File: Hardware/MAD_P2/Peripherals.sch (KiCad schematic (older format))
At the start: 24 parts

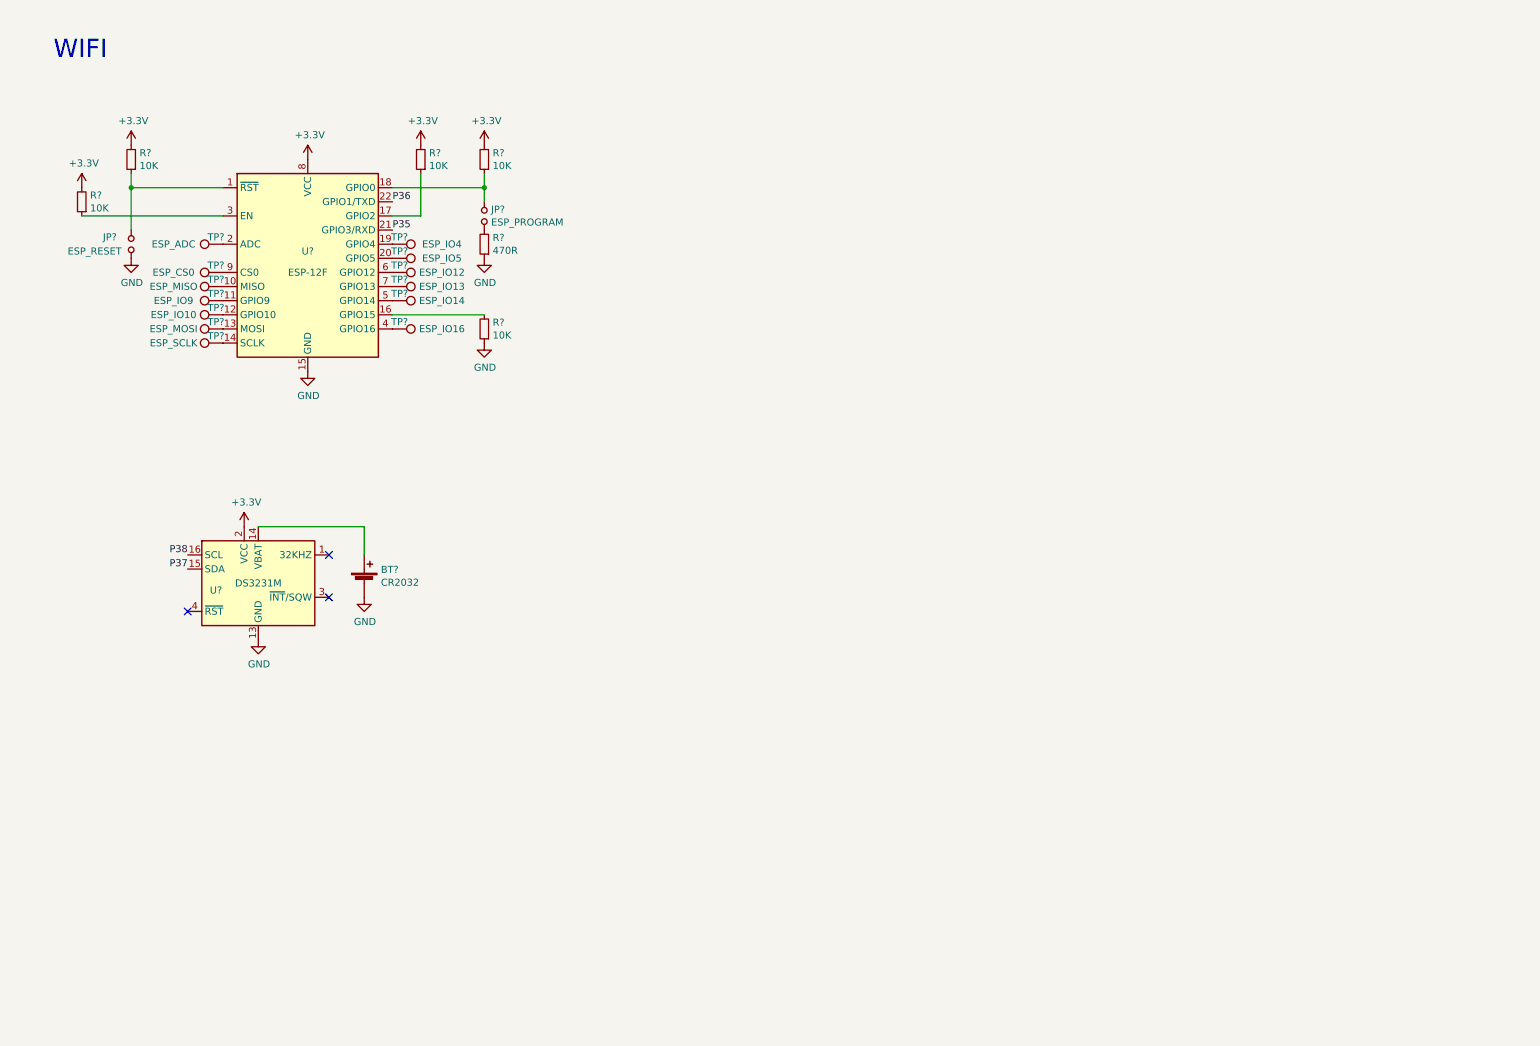
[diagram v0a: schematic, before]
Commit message: added adc
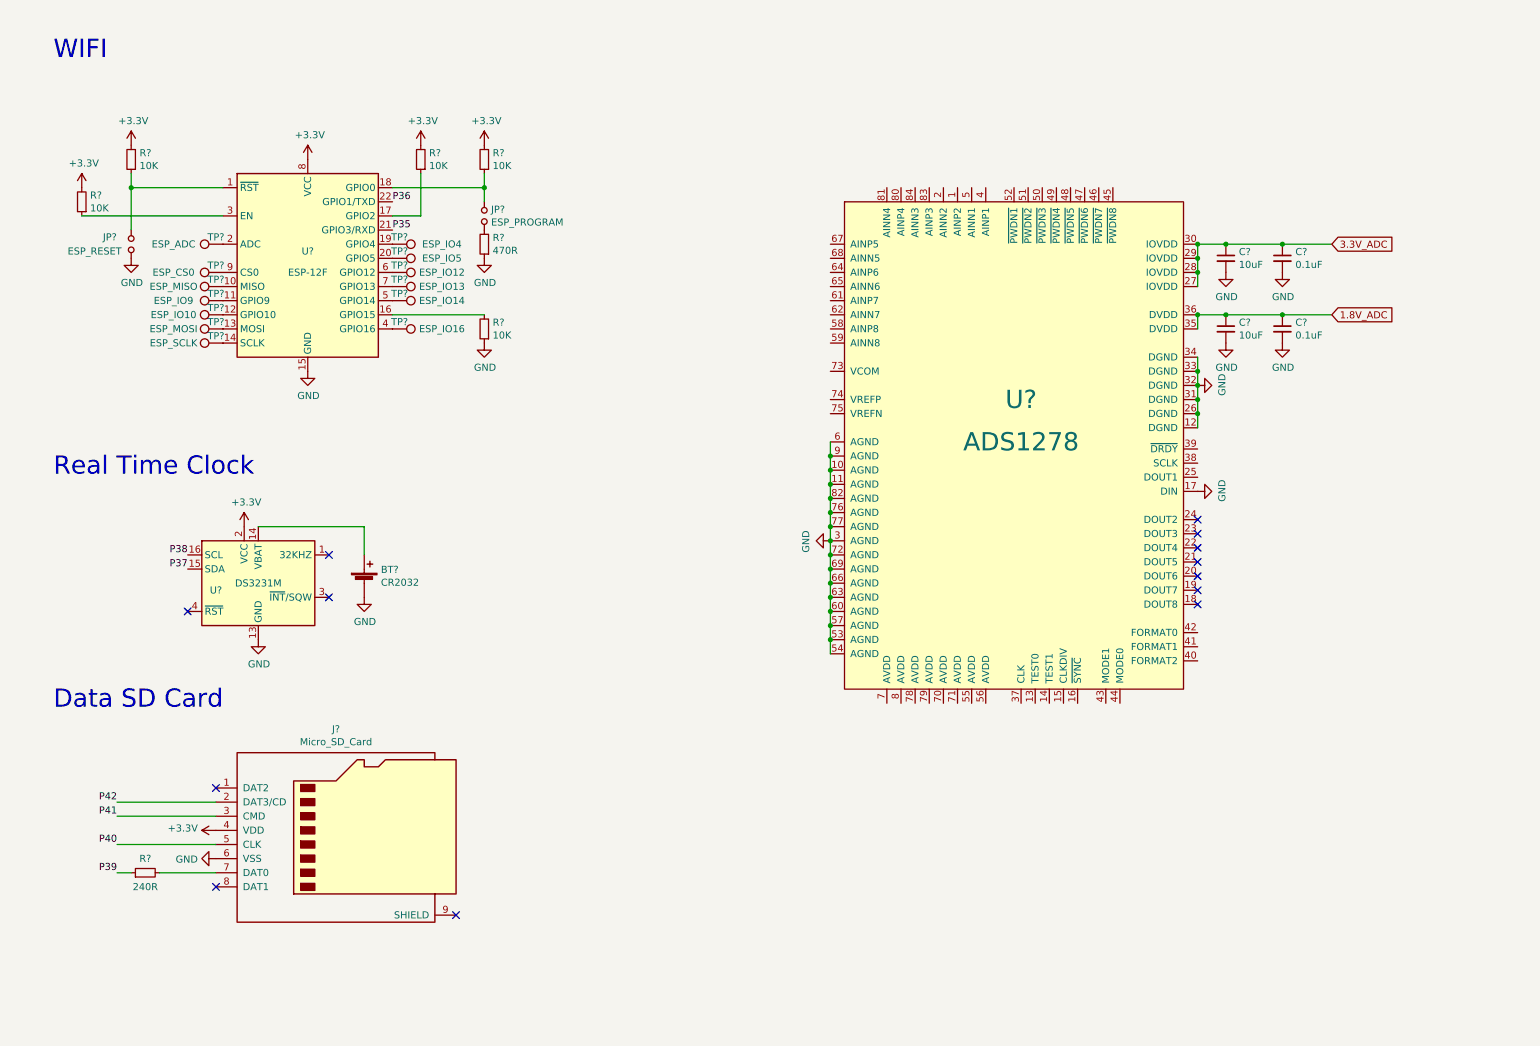
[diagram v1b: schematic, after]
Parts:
- added C? (x2): 10uF, symbol Device:C_Small
- added C? (x2): 0.1uF, symbol Device:C_Small
- added J?: Micro_SD_Card, symbol Connector:Micro_SD_Card
- added R?: 240R, symbol Device:R_Small
- added U?: ADS1278, symbol MAD_P2-rescue:ADS1278-REF
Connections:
- net +3V3: now also J?.4 (VDD)
- net GND: now also C?.2, C?.2, C?.2, C?.2, J?.6 (VSS), U?.10 (AGND), U?.11 (AGND), U?.12 (DGND), U?.17 (DIN), U?.26 (DGND), U?.3 (AGND), U?.31 (DGND), U?.32 (DGND), U?.33 (DGND), U?.34 (DGND), U?.53 (AGND), U?.54 (AGND), U?.57 (AGND), U?.6 (AGND), U?.60 (AGND), U?.63 (AGND), U?.66 (AGND), U?.69 (AGND), U?.72 (AGND), U?.76 (AGND), U?.77 (AGND), U?.82 (AGND), U?.9 (AGND)
- new net: J?.7 (DAT0), R?.2
- new net 1.8V_ADC: C?.1, C?.1, U?.35 (DVDD), U?.36 (DVDD)
- new net 3.3V_ADC: C?.1, C?.1, U?.27 (IOVDD), U?.28 (IOVDD), U?.29 (IOVDD), U?.30 (IOVDD)
- new net P39: R?.1
- new net P40: J?.5 (CLK)
- new net P41: J?.3 (CMD)
- new net P42: J?.2 (DAT3/CD)
- no-connect marks 3 -> 13
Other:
- note added: "Data SD Card"
- note added: "Real Time Clock"

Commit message: changed adc to ads131
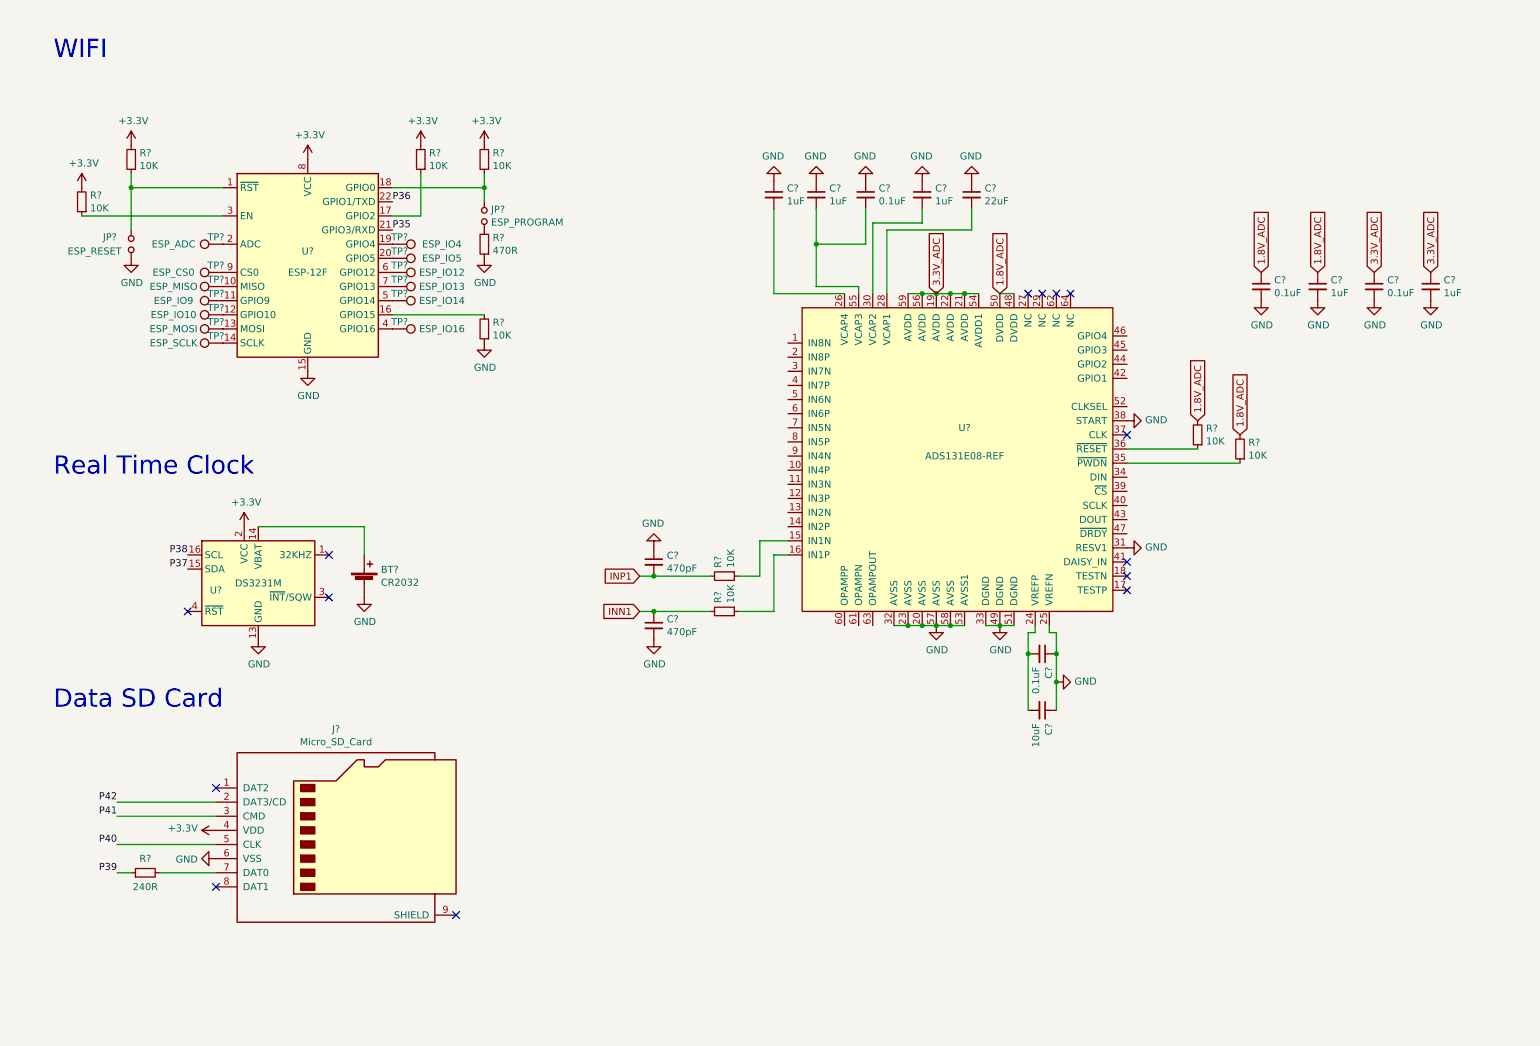
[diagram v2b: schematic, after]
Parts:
- removed C? (x2): 10uF, symbol Device:C_Small
- removed C? (x2): 0.1uF, symbol Device:C_Small
- removed U?: ADS1278, symbol MAD_P2-rescue:ADS1278-REF
- added C? (x4): 0.1uF, symbol Device:C_Small
- added C? (x5): 1uF, symbol Device:C_Small
- added C?: 22uF, symbol Device:C_Small
- added C?: 10uF, symbol Device:C_Small
- added C? (x2): 470pF, symbol Device:C_Small
- added R? (x4): 10K, symbol Device:R_Small
- added U?: ADS131E08-REF, symbol MAD_P2-rescue:ADS131E08-REF
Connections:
- net 1.8V_ADC: now also C?.1, C?.1, R?.2, R?.2, U?.48 (DVDD), U?.50 (DVDD)
- net 3.3V_ADC: now also C?.1, C?.1, U?.19 (AVDD), U?.21 (AVDD), U?.22 (AVDD), U?.54 (AVDD1), U?.56 (AVDD), U?.59 (AVDD)
- net GND: now also C?.1, C?.1, C?.1, C?.1, C?.1, C?.1, C?.1, C?.1, C?.2, C?.2, C?.2, C?.2, C?.2, U?.20 (AVSS), U?.23 (AVSS), U?.25 (VREFN), U?.31 (RESV1), U?.32 (AVSS), U?.33 (DGND), U?.38 (START), U?.49 (DGND), U?.51 (DGND), U?.53 (AVSS1), U?.57 (AVSS), U?.58 (AVSS)
- new net: R?.1, U?.15 (IN1N)
- new net: R?.1, U?.16 (IN1P)
- new net: C?.2, C?.2, U?.24 (VREFP)
- new net: C?.2, U?.26 (VCAP4)
- new net: C?.2, U?.28 (VCAP1)
- new net: C?.2, U?.30 (VCAP2)
- new net: R?.1, U?.35 (~PWDN)
- new net: R?.1, U?.36 (~RESET)
- new net: C?.2, C?.2, U?.55 (VCAP3)
- new net INN1: C?.1, R?.2
- new net INP1: C?.2, R?.2
- no-connect marks 13 -> 14

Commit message: finished adc, added dac
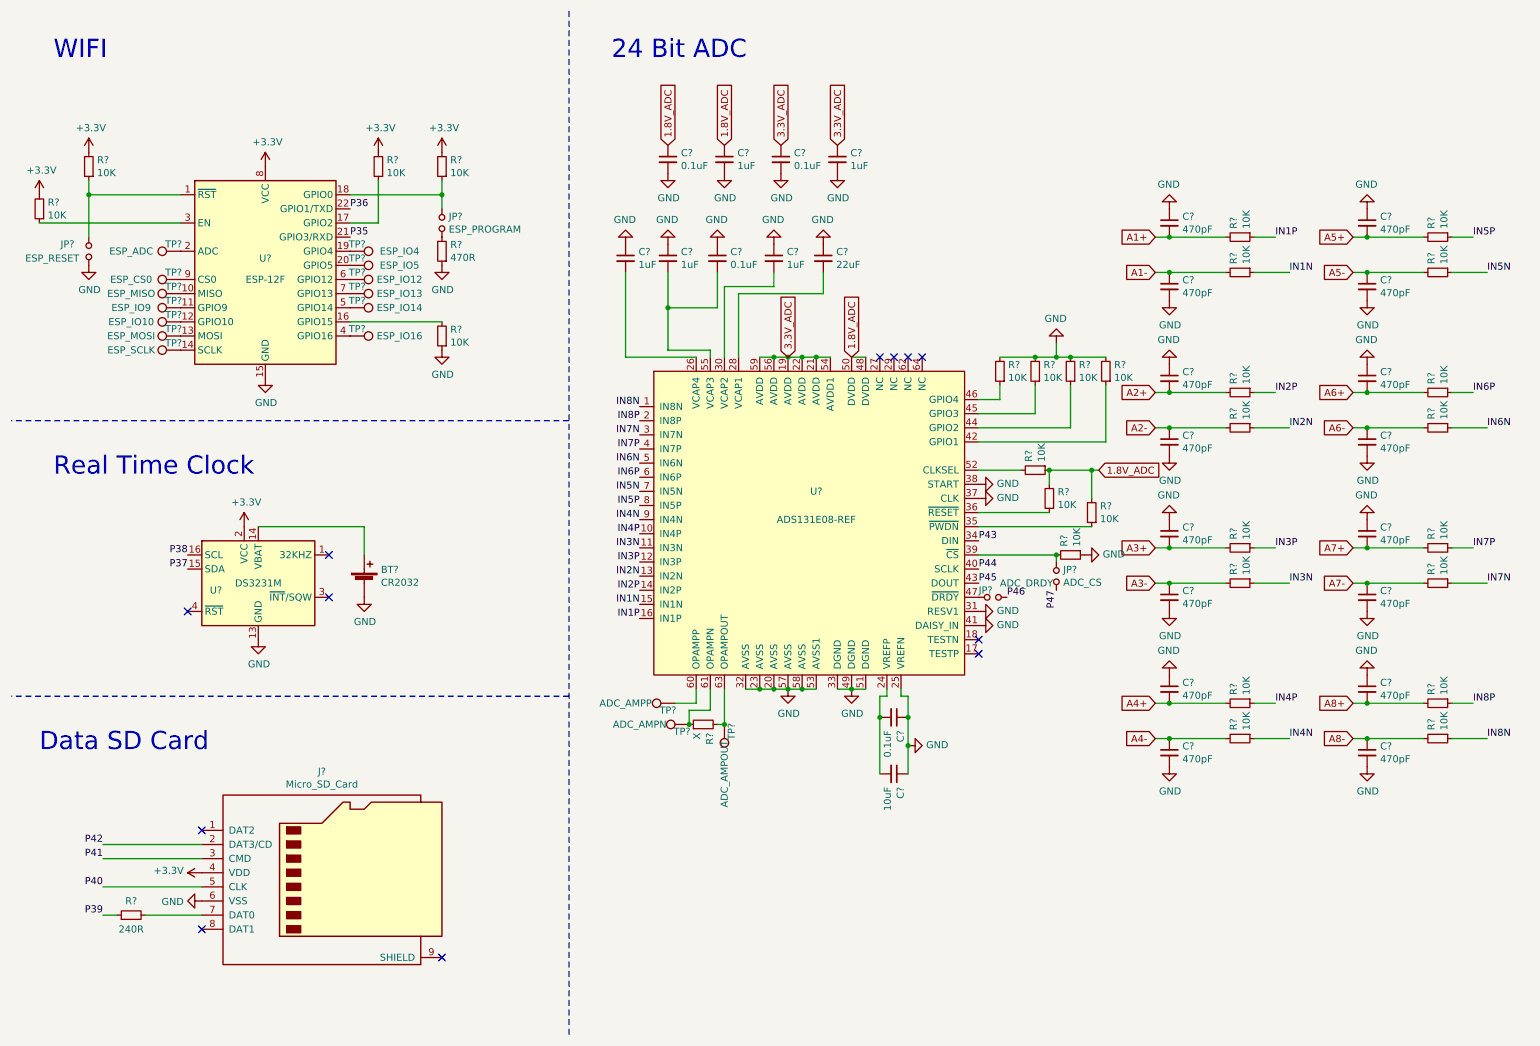
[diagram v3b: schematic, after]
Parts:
- removed C? (x2): 470pF, symbol Device:C_Small
- removed R? (x2): 10K, symbol Device:R_Small
- added C? (x16): 470pF, symbol Device:C_Small
- added JP?: ADC_CS, symbol Device:Jumper_NO_Small
- added JP?: ADC_DRDY, symbol Device:Jumper_NO_Small
- added R? (x22): 10K, symbol Device:R_Small
- added R?: X, symbol Device:R_Small
- added TP?: ADC_AMPP, symbol Connector:TestPoint
- added TP?: ADC_AMPN, symbol Connector:TestPoint
- added TP?: ADC_AMPOUT, symbol Connector:TestPoint
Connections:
- net 1.8V_ADC: now also R?.1
- net GND: now also U?.37 (CLK), U?.41 (DAISY_IN), C?.1, C?.1, C?.1, C?.1, C?.1, C?.1, C?.1, C?.1, C?.2, C?.2, C?.2, C?.2, C?.2, C?.2, C?.2, C?.2, R?.1, R?.2, R?.2, R?.2, R?.2
- net IN8N: now reaches U?.1 (IN8N)
- net IN8N: now also R?.1
- net IN4P: now reaches U?.10 (IN4P)
- net IN4P: now also R?.1
- net IN3N: now reaches U?.11 (IN3N)
- net IN3N: now also R?.1
- net IN3P: now reaches U?.12 (IN3P)
- net IN3P: now also R?.1
- net IN2N: now reaches U?.13 (IN2N)
- net IN2N: now also R?.1
- net IN2P: now reaches U?.14 (IN2P)
- net IN2P: now also R?.1
- net IN1N: now reaches U?.15 (IN1N)
- net IN1N: now also R?.1
- net IN1P: now reaches U?.16 (IN1P)
- net IN1P: now also R?.1
- net IN8P: now reaches U?.2 (IN8P)
- net IN8P: now also R?.1
- net IN7N: now reaches U?.3 (IN7N)
- net IN7N: now also R?.1
- net P43: now reaches U?.34 (DIN)
- net at U?.39 (~CS): now also JP?.1, R?.2
- net IN7P: now reaches U?.4 (IN7P)
- net IN7P: now also R?.1
- net P44: now reaches U?.40 (SCLK)
- net at U?.42 (GPIO1): now also R?.1
- net P45: now reaches U?.43 (DOUT)
- net at U?.44 (GPIO2): now also R?.1
- net at U?.45 (GPIO3): now also R?.1
- net at U?.46 (GPIO4): now also R?.1
- net at U?.47 (~DRDY): now also JP?.1
- net IN6N: now reaches U?.5 (IN6N)
- net IN6N: now also R?.1
- net at U?.52 (CLKSEL): now also R?.2
- net IN6P: now reaches U?.6 (IN6P)
- net IN6P: now also R?.1
- net at U?.60 (OPAMPP): now also TP?.1
- net at U?.61 (OPAMPN): now also R?.1, TP?.1
- net at U?.63 (OPAMPOUT): now also R?.2, TP?.1
- net IN5N: now reaches U?.7 (IN5N)
- net IN5N: now also R?.1
- net IN5P: now reaches U?.8 (IN5P)
- net IN5P: now also R?.1
- net IN4N: now reaches U?.9 (IN4N)
- net IN4N: now also R?.1
- new net A1+: C?.2, R?.2
- new net A1-: C?.1, R?.2
- new net A2+: C?.2, R?.2
- new net A2-: C?.1, R?.2
- new net A3+: C?.2, R?.2
- new net A3-: C?.1, R?.2
- new net A4+: C?.2, R?.2
- new net A4-: C?.1, R?.2
- new net A5+: C?.2, R?.2
- new net A5-: C?.1, R?.2
- new net A6+: C?.2, R?.2
- new net A6-: C?.1, R?.2
- new net A7+: C?.2, R?.2
- new net A7-: C?.1, R?.2
- new net A8+: C?.2, R?.2
- new net A8-: C?.1, R?.2
- new net P46: JP?.2
- new net P47: JP?.2
- no-connect marks 14 -> 12
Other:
- note added: "24 Bit ADC"
- moved on the sheet: C?, J?, JP?, R?, TP?, U?

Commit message: began pcb layout
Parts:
- BT1: renamed from BT?; footprint (none) -> Battery:BatteryHolder_Keystone_1058_1x2032
- C108, C109, C110, C111, C112, C113, C114, C115, C116, C117, C118, C119, C120, C121, C122, C123, C124, C125, C126, C127, C128, C129, C130, C131, C132, C133, C134: renamed from C?; footprint (none) -> Capacitor_SMD:C_0603_1608Metric
- J12: renamed from J?; footprint (none) -> Tensile_Board:WM26501
- JP18, JP19, JP20, JP21: renamed from JP?; footprint (none) -> Jumper:SolderJumper-2_P1.3mm_Open_Pad1.0x1.5mm
- R23, R24, R25, R26, R27, R28, R29, R30, R31, R32, R33, R34, R35, R36, R37, R38, R39, R40, R41, R42, R43, R44, R45, R46, R47, R48, R49, R50, R51, R52, R53, R54: renamed from R?; footprint (none) -> Resistor_SMD:R_0603_1608Metric
- TP1, TP10, TP11, TP12, TP13, TP14, TP15, TP16, TP2, TP3, TP4, TP5, TP6, TP7, TP8, TP9: renamed from TP?; footprint (none) -> TestPoint:TestPoint_Pad_1.0x1.0mm
- U30: renamed from U?; footprint (none) -> Package_QFP:TQFP-64_10x10mm_P0.5mm
- gave numbers to parts that had none: 2
